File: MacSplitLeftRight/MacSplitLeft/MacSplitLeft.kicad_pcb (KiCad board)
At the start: 2 copper layers, 166.1 x 112 mm, 75 parts, among them J1 AudioJack4, SW1 SW_Push, SW10 SW_Push, SW100 Toggle Mac/Win, SW11 SW_Push, SW12 SW_Push, SW13 SW_Push, SW14 SW_Push, SW15 SW_Push, SW16 SW_Push, SW17 SW_Push, SW18 SW_Push, SW19 SW_Push, SW2 SW_Push, SW20 SW_Push, SW21 SW_Push, SW22 SW_Push, SW23 SW_Push, SW24 SW_Push, SW25 SW_Push, SW26 SW_Push, SW27 SW_Push, SW28 SW_Push, SW29 SW_Push, SW3 SW_Push, SW30 SW_Push, SW4 SW_Push, SW5 SW_Push, SW6 SW_Push, SW7 SW_Push, SW8 SW_Push, SW9 SW_Push, U2 KB2040

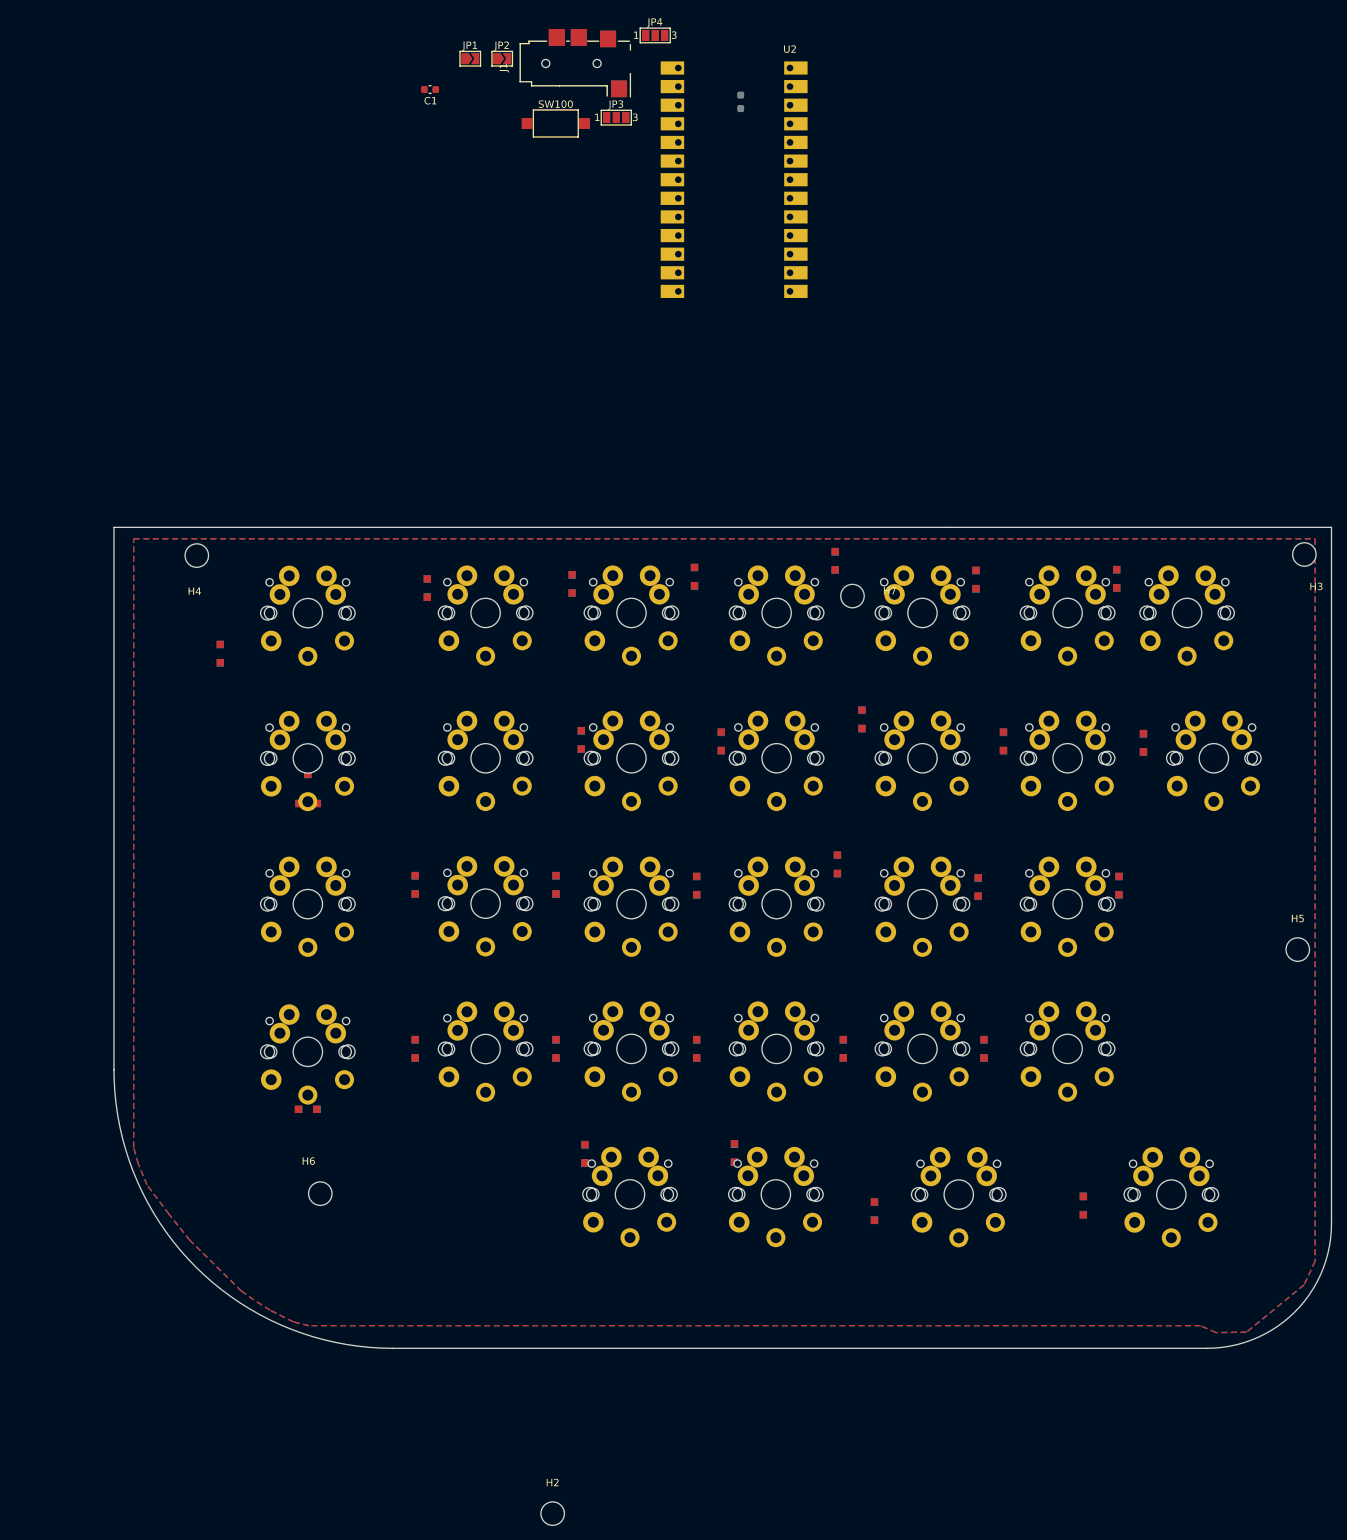
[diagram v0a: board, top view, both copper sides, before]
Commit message: Left 32 keys
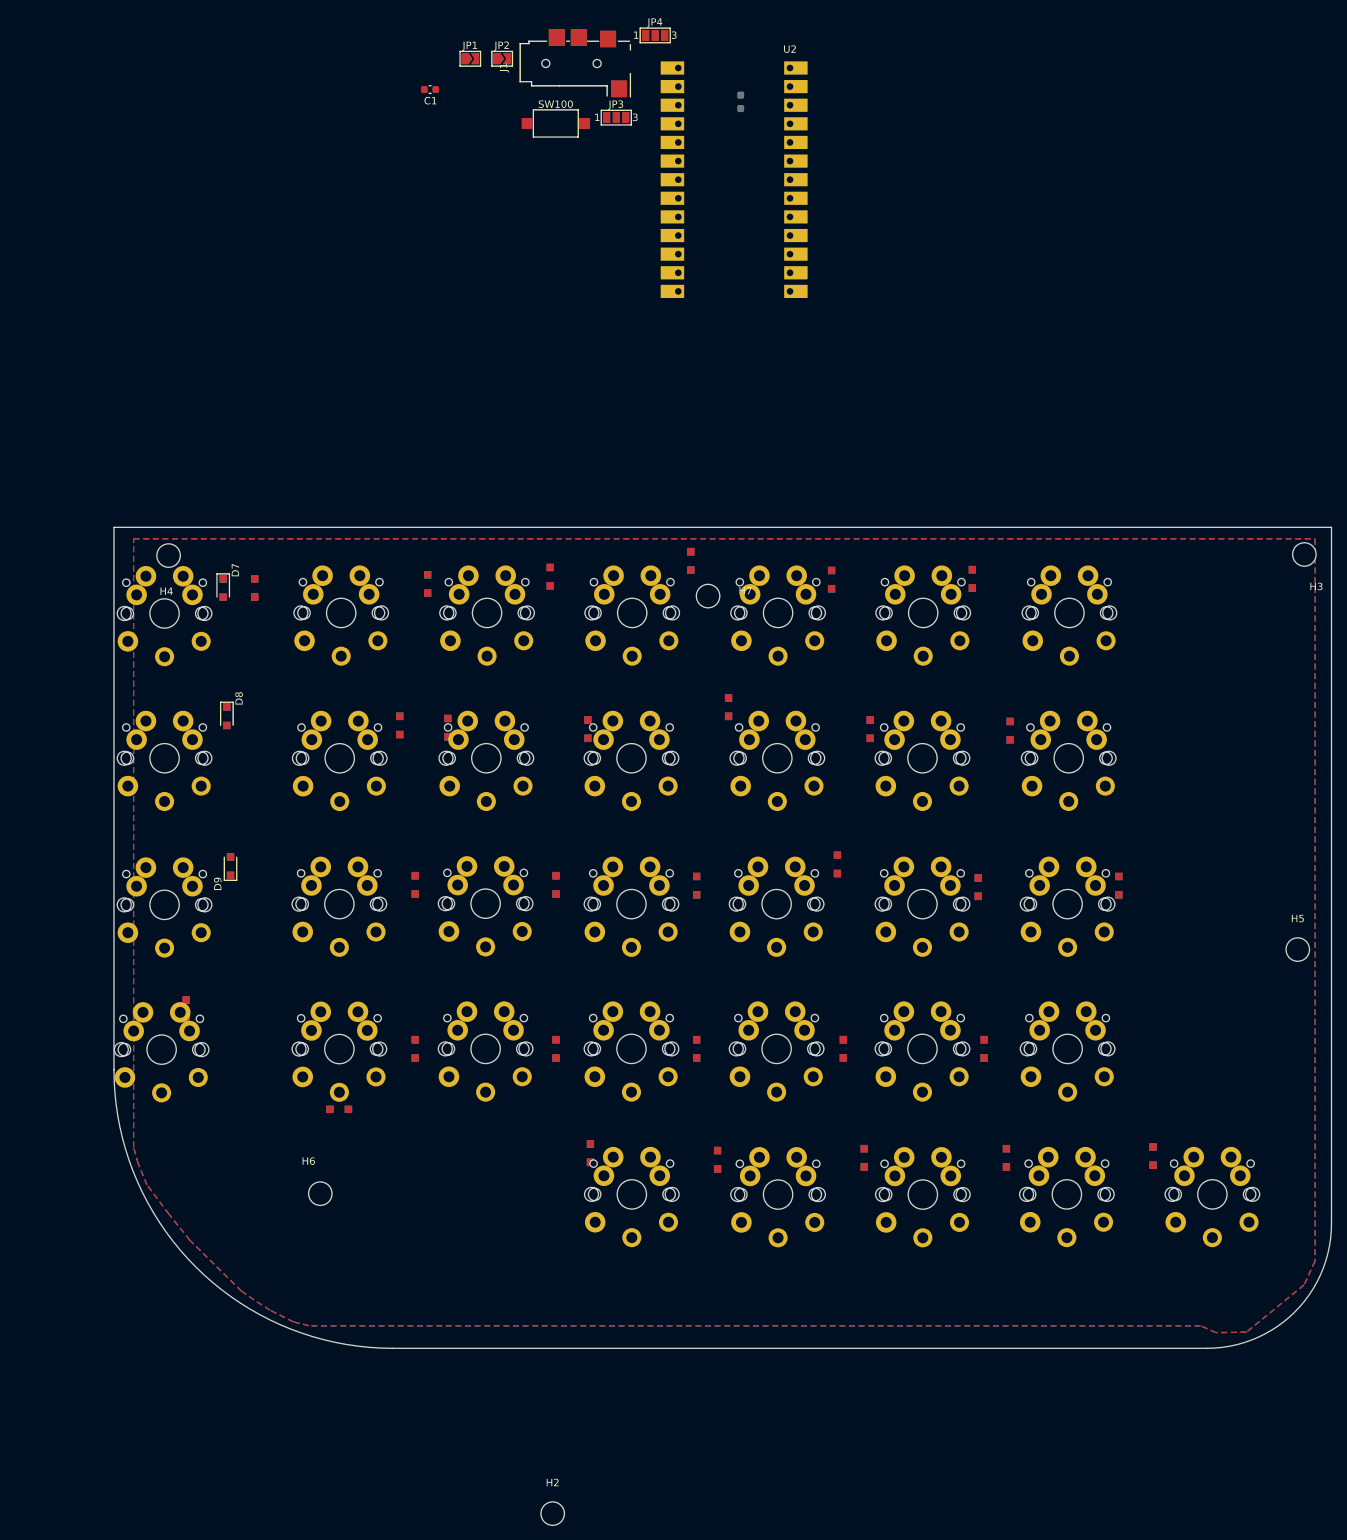
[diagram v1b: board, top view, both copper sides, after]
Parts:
- added D7: 1N4148W, Diode_SMD:D_SOD-323_Hand_Split_Keyboard, F.Cu at (101.4, 43.2)
- added D8: 1N4148W, Diode_SMD:D_SOD-323_Hand_Split_Keyboard, F.Cu at (101.9, 60.8)
- added D9: 1N4148W, Diode_SMD:D_SOD-323_Hand_Split_Keyboard, F.Cu at (102.4, 81.2)
- added SW31: SW_Push, Lily58-footprint:MX_PG1350-DoubleSide_Keycap_28mm_1.50u, F.Cu at (93.4, 46.8)
- added SW32: SW_Push, Lily58-footprint:MX_PG1350-DoubleSide_Keycap_28mm_1.50u, F.Cu at (93.4, 66.5)
- added SW33: SW_Push, Lily58-footprint:MX_PG1350-DoubleSide_Keycap_28mm_1.50u, F.Cu at (93.4, 86.5)
- SW13, SW19, SW27, SW28, SW29, SW30: footprint Lily58-footprint:MX_PG1350-DoubleSide_Keycap_28mm_1.50u -> Lily58-footprint:MX_PG1350-DoubleSide_Keycap_18mm_1.00u
- SW25: footprint Lily58-footprint:MX_PG1350-DoubleSide_Keycap_18mm_1.00u -> Lily58-footprint:MX_PG1350-DoubleSide_Keycap_28mm_1.50u
- moved SW30 137.0 mm to (236.3, 126.0)
- moved SW29 130.4 mm to (216.5, 126.0)
- moved D32 127.4 mm to (208.2, 121.0), turned to -90 degrees
- moved D33 124.9 mm to (228.2, 120.8), turned to -90 degrees
- moved SW25 66.9 mm to (93.0, 106.2)
- moved D28 57.9 mm to (96.3, 100.8)
- moved SW28 33.9 mm to (196.8, 126.0)
- moved D31 30.6 mm to (188.8, 121.0)
- moved SW27 24.7 mm to (177.1, 126.0)
- moved D1 23.5 mm to (105.7, 43.2)
- moved D30 22.5 mm to (168.8, 121.2)
- moved SW7 19.9 mm to (117.3, 66.5)
- moved SW10 19.8 mm to (177.0, 66.5)
- moved SW11 19.8 mm to (196.8, 66.5)
- moved SW12 19.8 mm to (216.8, 66.5)
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
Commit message: Position readjustments
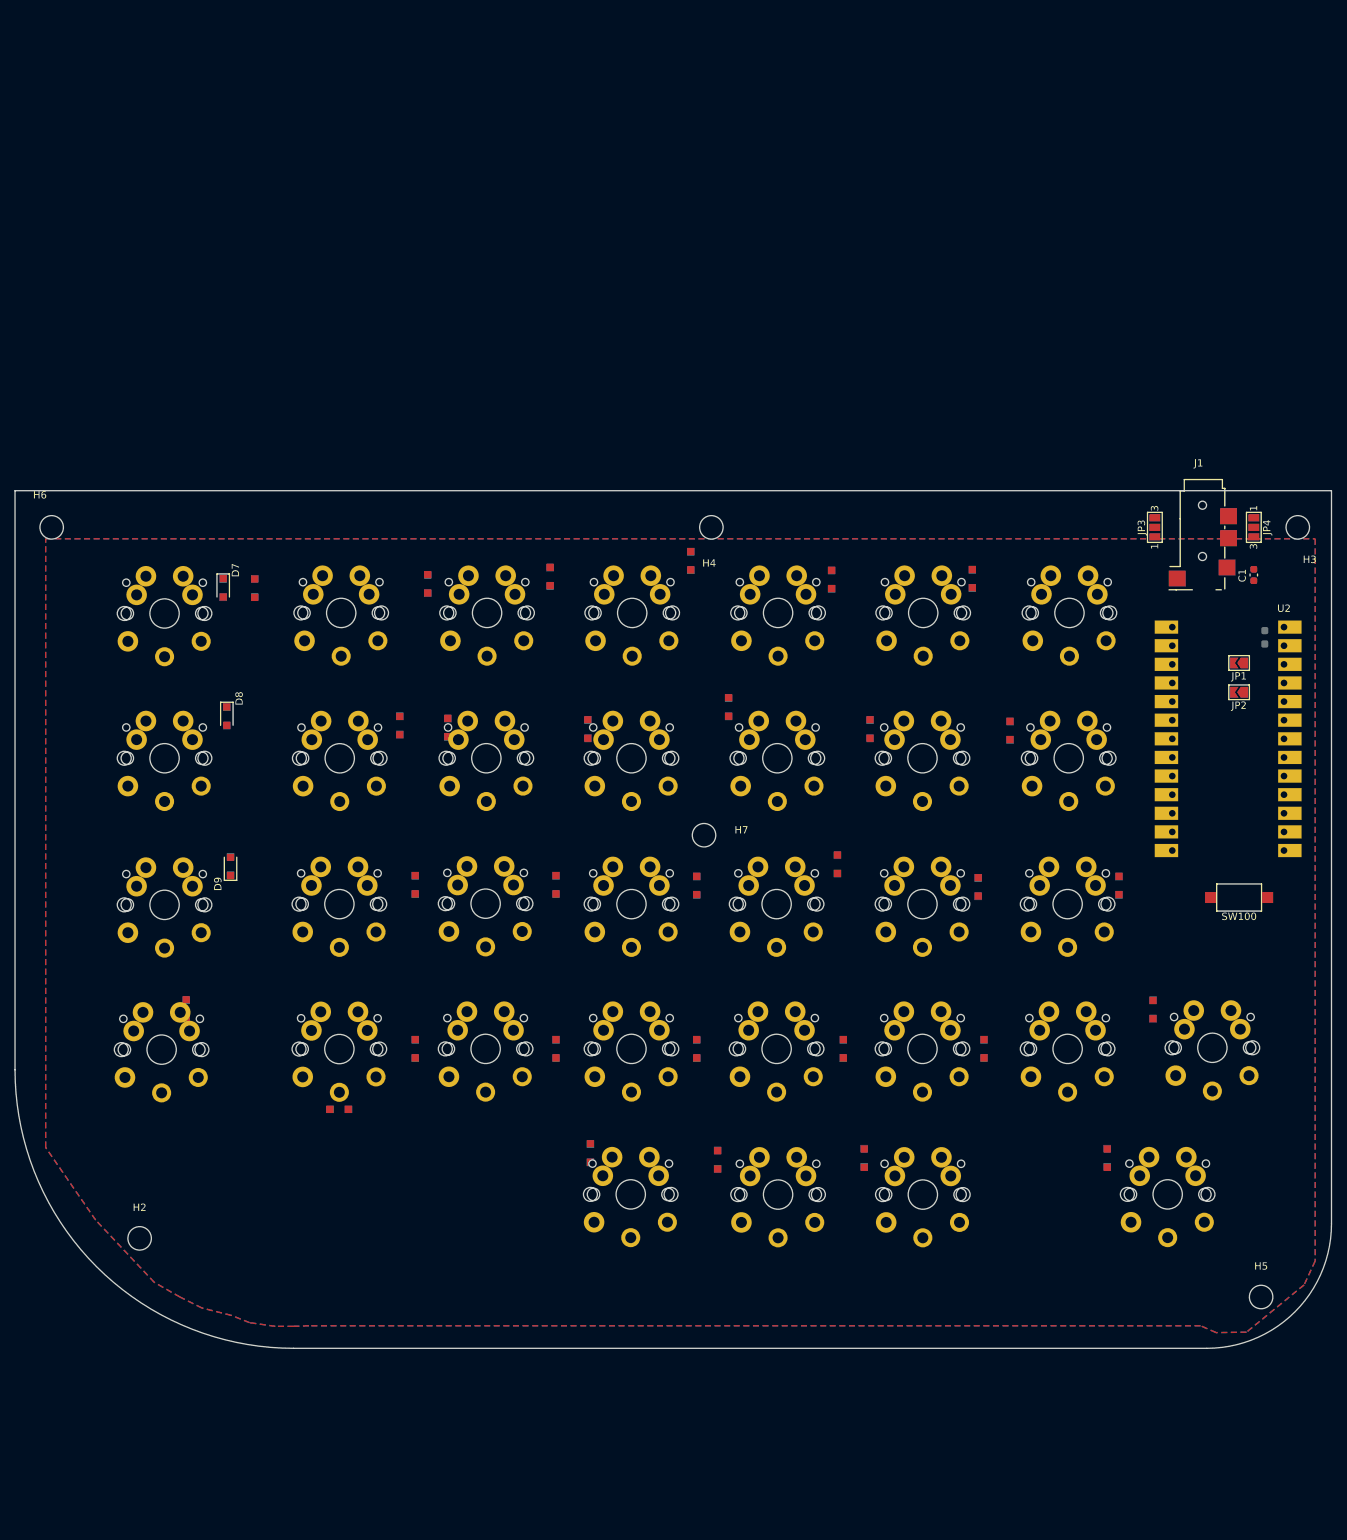
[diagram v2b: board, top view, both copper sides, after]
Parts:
- SW29: footprint Lily58-footprint:MX_PG1350-DoubleSide_Keycap_18mm_1.00u -> Lily58-footprint:MX_PG1350-DoubleSide_Keycap_28mm_1.50u
- moved SW100 140.9 mm to (240.0, 85.5), turned to 180 degrees
- moved JP1 133.4 mm to (240.0, 53.5), turned to 180 degrees
- moved JP2 132.6 mm to (240.0, 57.5), turned to 180 degrees
- moved C1 130.4 mm to (242.0, 41.5), turned to -90 degrees
- moved J1 108.6 mm to (235.0, 29.7), turned to -90 degrees
- moved JP4 105.7 mm to (242.0, 35.0), turned to -90 degrees
- moved R1 102.2 mm to (243.5, 50.0), turned to 90 degrees
- moved U2 101.8 mm to (238.5, 48.6)
- moved H6 98.0 mm to (78.0, 35.0)
- moved JP3 92.3 mm to (228.5, 35.0), turned to 90 degrees
- moved H4 74.1 mm to (168.0, 35.0)
- moved H2 67.7 mm to (90.0, 132.0)
- moved H5 47.7 mm to (243.0, 140.0)
- moved H7 32.6 mm to (167.0, 77.0)
- moved D33 20.0 mm to (228.2, 100.8)
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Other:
- board size 166.1 x 112 mm -> 179.6 x 117 mm
